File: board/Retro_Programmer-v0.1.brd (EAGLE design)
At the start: 45 x 45 mm, 48 parts, among them IC1 74LVC125A, K1 61301511821, K2 61301511821, P1 POWERSUPPLY_DC21MMX, Q1 BC857CSMD, SW1 SPUSH, SW2 SPUSH, SW3 SPUSH, SW4 SLIDE_WAY4, T2 BC847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

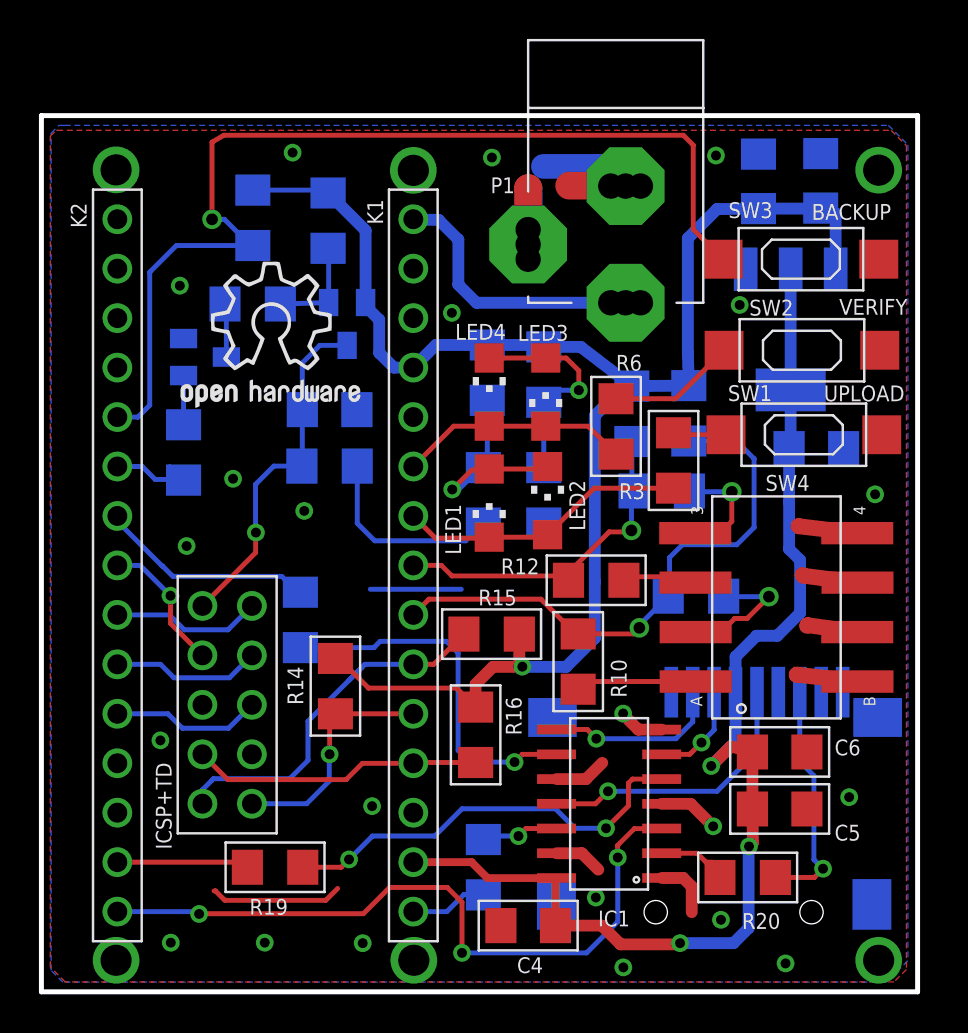
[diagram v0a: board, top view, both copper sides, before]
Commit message: improved labelling on board
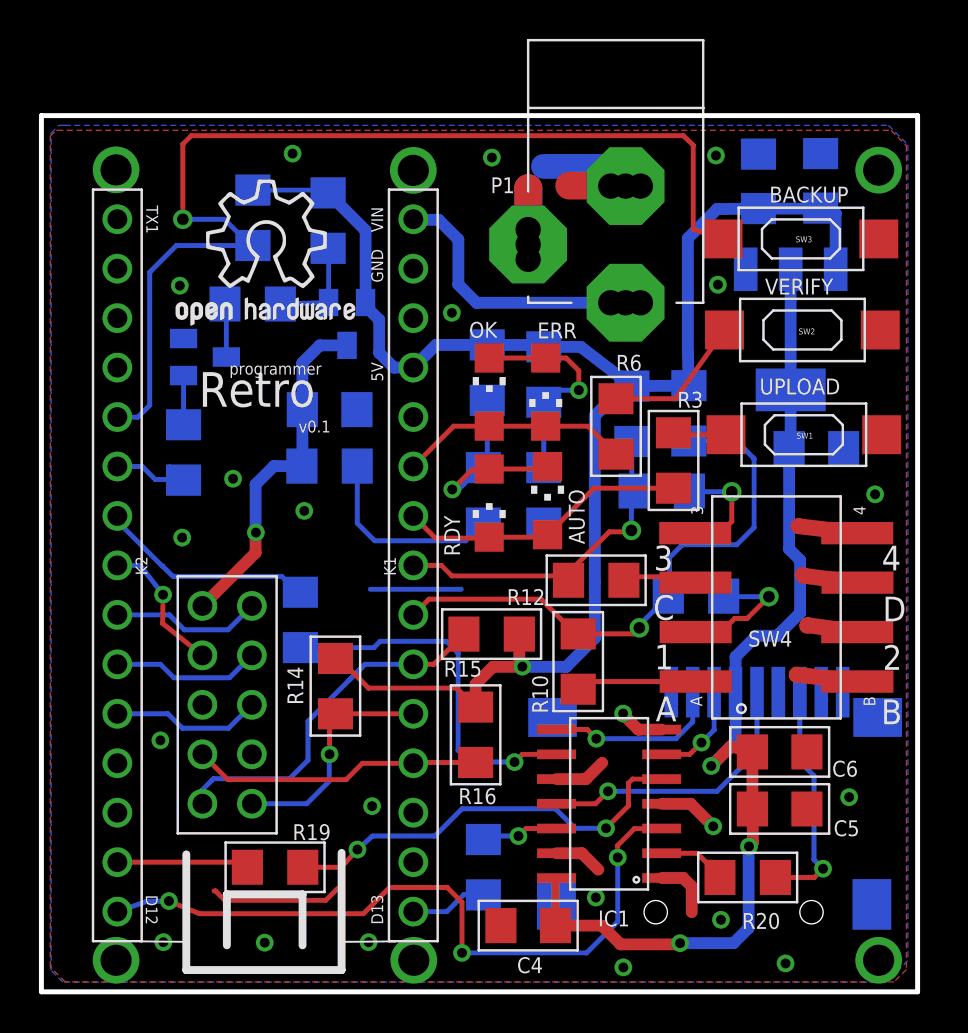
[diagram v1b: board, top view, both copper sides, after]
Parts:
- R11, R13: value 22K -> 10K
- moved SW2 1.04 mm to (39.1, 34.0)
- moved SW3 1.04 mm to (39.0, 38.7)
- renumbered LED1 to RDY, LED2 to AUTO, LED3 to ERR, LED4 to OK, T2 to Q2
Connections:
- net +3V3: no longer K1.14
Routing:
- net +3V3: track 61.9 -> 54.2 mm
- net D2: track 53.5 -> 55.9 mm
- net N$4: track 6.58 -> 7.39 mm
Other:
- board text added: "1"
- board text added: "2"
- board text added: "3"
- board text added: "4"
- board text added: "5V"
- board text added: "A"
- board text added: "B"
- board text added: "C"
- board text added: "D"
- board text added: "D12"
- board text added: "D13"
- board text added: "GND"
- board text added: "Retro"
- board text added: "TX1"
- board text added: "VIN"
- board text added: "programmer"
- board text added: "v0.1"

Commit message: font changes
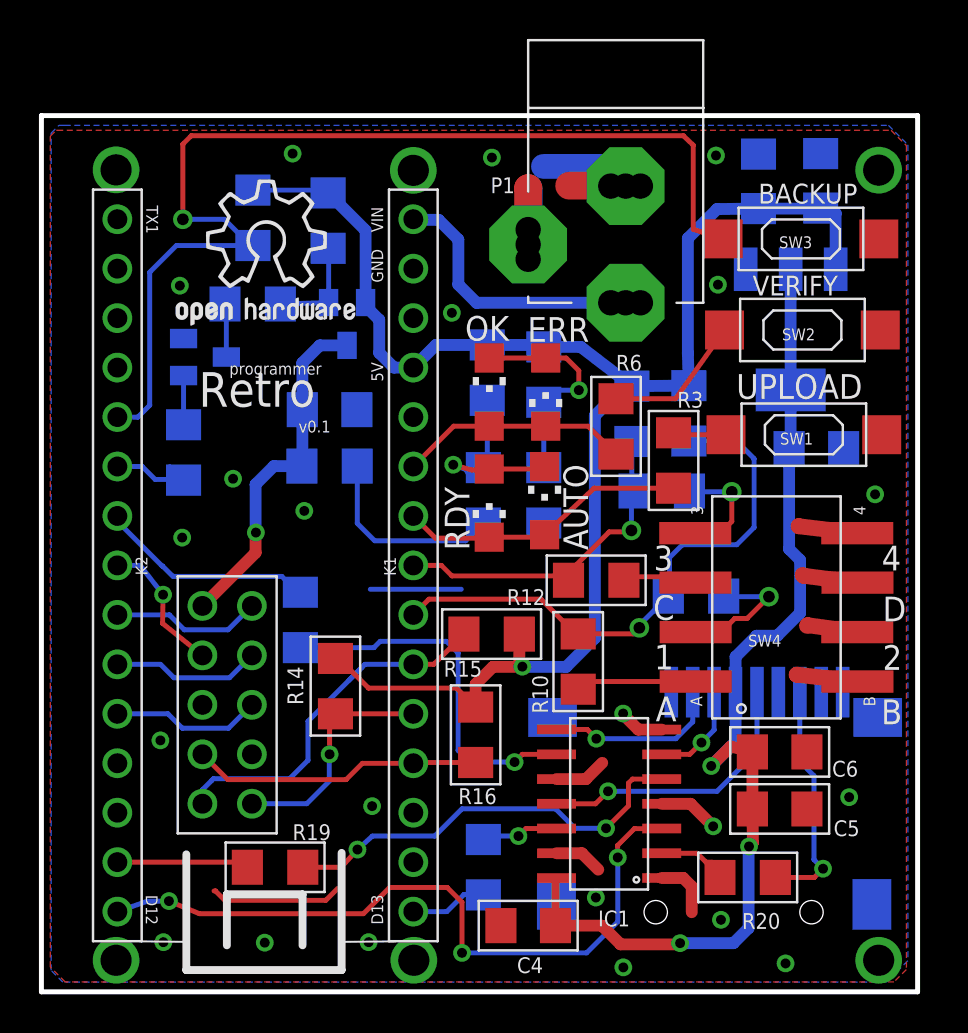
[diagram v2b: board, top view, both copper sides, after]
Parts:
- moved AUTO 0.15 mm to (25.8, 25.2)
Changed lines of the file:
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@@
 <setting verticaltext="up"/>
 </settings>
-<grid distance="1" unitdist="mil" unit="mm" style="lines" multiple="1" display="yes" altdistance="0.025" altunitdist="inch" altunit="inch"/>
+<grid distance="2.54" unitdist="mm" unit="mm" style="lines" multiple="1" display="yes" altdistance="0.025" altunitdist="inch" altunit="inch"/>
 <layers>
 <layer number="1" name="Top" color="4" fill="1" visible="yes" active="yes"/>
-<layer number="16" name="Bottom" color="1" fill="1" visible="yes" active="yes"/>
+<layer number="16" name="Bottom" color="1" fill="1" visible="no" active="yes"/>
 <layer number="17" name="Pads" color="2" fill="1" visible="yes" active="yes"/>
 <layer number="18" name="Vias" color="2" fill="1" visible="yes" active="yes"/>
@@
 <circle x="19.118" y="1.5652" radius="0.943909375" width="0.254" layer="49"/>
 <circle x="3.8526" y="1.5906" radius="0.915809375" width="0.254" layer="49"/>
-<text x="36.2966" y="17.7292" size="0.8128" layer="25">SW4</text>
-<text x="41.4528" y="41.3512" size="0.8128" layer="25" rot="R180">BACKUP</text>
-<text x="37.1602" y="35.814" size="0.8128" layer="25">VERIFY</text>
-<text x="36.8808" y="30.6832" size="0.8128" layer="25">UPLOAD</text>
+<text x="36.2966" y="17.7292" size="0.6096" layer="25">SW4</text>
+<text x="41.91" y="41.5036" size="1.016" layer="25" font="vector" ratio="16" rot="R180">BACKUP</text>
+<text x="36.5252" y="35.7632" size="1.016" layer="25" font="vector" ratio="16">VERIFY</text>
+<text x="35.687" y="30.4546" size="1.27" layer="25" font="vector" ratio="16">UPLOAD</text>
 <rectangle x1="58.78195" y1="33.206690625" x2="58.82766875" y2="33.214309375" layer="200"/>
 <rectangle x1="58.77433125" y1="33.214309375" x2="58.85053125" y2="33.221928125" layer="200"/>
@@
 </element>
 <element name="RDY" library="led" package="CHIPLED_1206" value="YEL" x="23" y="25.1" smashed="yes" rot="R180">
-<attribute name="NAME" x="21.5008" y="22.3726" size="0.8128" layer="25" rot="R90"/>
+<attribute name="NAME" x="21.9834" y="22.6774" size="1.27" layer="25" font="vector" ratio="16" rot="R90"/>
 <attribute name="VALUE" x="20.46" y="26.37" size="1.27" layer="27" rot="R270"/>
 </element>
-<element name="AUTO" library="led" package="CHIPLED_1206" value="GRE" x="25.9952" y="25.2254" smashed="yes">
-<attribute name="NAME" x="27.9002" y="22.9902" size="0.8128" layer="25" rot="R90"/>
-<attribute name="VALUE" x="28.5352" y="23.9554" size="1.27" layer="27" rot="R90"/>
+<element name="AUTO" library="led" package="CHIPLED_1206" value="GRE" x="25.8428" y="25.2254" smashed="yes">
+<attribute name="NAME" x="28.078" y="22.6854" size="1.27" layer="25" font="vector" ratio="16" rot="R90"/>
+<attribute name="VALUE" x="28.3828" y="23.9554" size="1.27" layer="27" rot="R90"/>
 </element>
 <element name="ERR" library="led" package="CHIPLED_1206" value="GRE" x="25.9" y="30.8" smashed="yes" rot="R180">
-<attribute name="NAME" x="27.498" y="34.3742" size="0.8128" layer="25" rot="R180"/>
+<attribute name="NAME" x="28.133" y="34.6536" size="1.27" layer="25" font="vector" ratio="16" rot="R180"/>
 <attribute name="VALUE" x="23.36" y="32.07" size="1.27" layer="27" rot="R270"/>
 </element>
 <element name="OK" library="led" package="CHIPLED_1206" value="RED" x="23" y="30.8" smashed="yes">
-<attribute name="NAME" x="21.9608" y="33.5912" size="0.8128" layer="25"/>
+<attribute name="NAME" x="21.7576" y="33.4388" size="1.27" layer="25" font="vector" ratio="16"/>
 <attribute name="VALUE" x="25.54" y="29.53" size="1.27" layer="27" rot="R90"/>
 </element>
@@
 </element>
 <element name="SW1" library="Ard" package="SLIDE1" value="SPUSH" x="39.1574" y="28.6116" smashed="yes" rot="R90">
-<attribute name="NAME" x="39.632" y="28.716" size="0.3048" layer="25" rot="R180"/>
+<attribute name="NAME" x="39.632" y="28.716" size="0.6096" layer="25" rot="R180"/>
 </element>
 <element name="SW2" library="Ard" package="SLIDE1" value="SPUSH" x="39.0844" y="33.9906" smashed="yes" rot="R90">
-<attribute name="NAME" x="39.7368" y="34.0696" size="0.3048" layer="25" rot="R180"/>
+<attribute name="NAME" x="39.7368" y="34.0696" size="0.6096" layer="25" rot="R180"/>
 </element>
 <element name="SW3" library="Ard" package="SLIDE1" value="SPUSH" x="39.0082" y="38.6698" smashed="yes" rot="R90">
-<attribute name="NAME" x="39.5844" y="38.7996" size="0.3048" layer="25" rot="R180"/>
+<attribute name="NAME" x="39.5844" y="38.7996" size="0.6096" layer="25" rot="R180"/>
 </element>
 <element name="SW4" library="Ard" package="SLIDESWITCH_4" value="SLIDE_WAY4" x="37.75" y="19.7444" smashed="yes" rot="R90"/>
@@
 <wire x1="22.95" y1="23.3" x2="20.24" y2="23.3" width="0.254" layer="1"/>
 <wire x1="23" y1="23.35" x2="25.8698" y2="23.35" width="0.254" layer="1"/>
-<wire x1="25.8698" y1="23.35" x2="25.9952" y2="23.4754" width="0.254" layer="1"/>
+<wire x1="25.8698" y1="23.35" x2="25.8428" y2="23.4754" width="0.254" layer="1"/>
 <wire x1="20.24" y1="23.3" x2="19.1" y2="24.44" width="0.254" layer="1"/>
 <wire x1="32.4664" y1="25.8674" x2="28.3872" y2="25.8674" width="0.254" layer="1"/>
-<wire x1="28.3872" y1="25.8674" x2="25.9952" y2="23.4754" width="0.254" layer="1"/>
+<wire x1="28.3872" y1="25.8674" x2="25.8428" y2="23.4754" width="0.254" layer="1"/>
 </signal>
 <signal name="A4">
@@
 <wire x1="16.65" y1="35.4" x2="16.65" y2="39.1038" width="0.6096" layer="16"/>
 <wire x1="16.65" y1="39.1038" x2="14.7254" y2="41.0284" width="0.6096" layer="16"/>
-<wire x1="28.4226" y1="29.591" x2="28.4226" y2="21.0566" width="0.6096" layer="16"/>
+<wire x1="28.4226" y1="29.591" x2="28.4226" y2="18.161" width="0.6096" layer="16"/>
 <wire x1="10.8588" y1="41.1734" x2="14.5804" y2="41.1734" width="0.254" layer="16"/>
 <wire x1="14.5804" y1="41.1734" x2="14.7254" y2="41.0284" width="0.254" layer="16"/>
@@
 <wire x1="19.1" y1="32.06" x2="18.105" y2="32.06" width="0.6096" layer="16"/>
 <wire x1="18.105" y1="32.06" x2="17.3482" y2="32.8168" width="0.6096" layer="16"/>
-<wire x1="28.4226" y1="21.0566" x2="28.4226" y2="18.161" width="0.6096" layer="16"/>
 <wire x1="28.4226" y1="18.161" x2="26.9494" y2="16.6878" width="0.6096" layer="16"/>
 <wire x1="26.9494" y1="16.6878" x2="24.7122" y2="16.6878" width="0.6096" layer="16"/>
@@
 <wire x1="22.9" y1="27.122" x2="22.7" y2="26.922" width="0.254" layer="16"/>
 <wire x1="23" y1="26.85" x2="26.2" y2="26.85" width="0.254" layer="1"/>
-<wire x1="26.2" y1="26.85" x2="25.9952" y2="26.9754" width="0.254" layer="1"/>
+<wire x1="26.2" y1="26.85" x2="25.8428" y2="26.9754" width="0.254" layer="1"/>
 <wire x1="22.9" y1="27.122" x2="22.622" y2="27.122" width="0.254" layer="16"/>
-<via x="21.1" y="25.8" extent="1-16" drill="0.508"/>
+<via x="21.1508" y="27.07" extent="1-16" drill="0.508"/>
 <wire x1="22.95" y1="26.8" x2="23" y2="26.85" width="0.254" layer="1"/>
 <wire x1="22.95" y1="26.8" x2="22.1" y2="26.8" width="0.254" layer="1"/>
-<wire x1="22.1" y1="26.8" x2="21.1" y2="25.8" width="0.254" layer="1"/>
-<wire x1="21.1" y1="25.8" x2="21.4312" y2="25.8" width="0.254" layer="16"/>
-<wire x1="21.4312" y1="25.8" x2="22.0218" y2="26.3906" width="0.254" layer="16"/>
+<wire x1="22.1" y1="26.8" x2="21.1508" y2="27.07" width="0.254" layer="1"/>
+<wire x1="21.1508" y1="27.07" x2="21.8122" y2="26.816" width="0.254" layer="16"/>
+<wire x1="21.8122" y1="26.816" x2="22.0218" y2="26.3906" width="0.254" layer="16"/>
 <wire x1="22.0218" y1="26.3906" x2="22.1686" y2="26.3906" width="0.254" layer="16"/>
 <wire x1="22.1686" y1="26.3906" x2="22.7" y2="26.922" width="0.254" layer="16"/>
